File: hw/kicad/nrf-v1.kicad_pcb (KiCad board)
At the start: 2 copper layers, 32 parts, among them U1 TPS62732, U2 nRF51822, U3 SST25WF040B, U4 BMA280, U5 SI7053, U6 BAL-NRF01D3, X1 16MHz, X2 32.768kHz

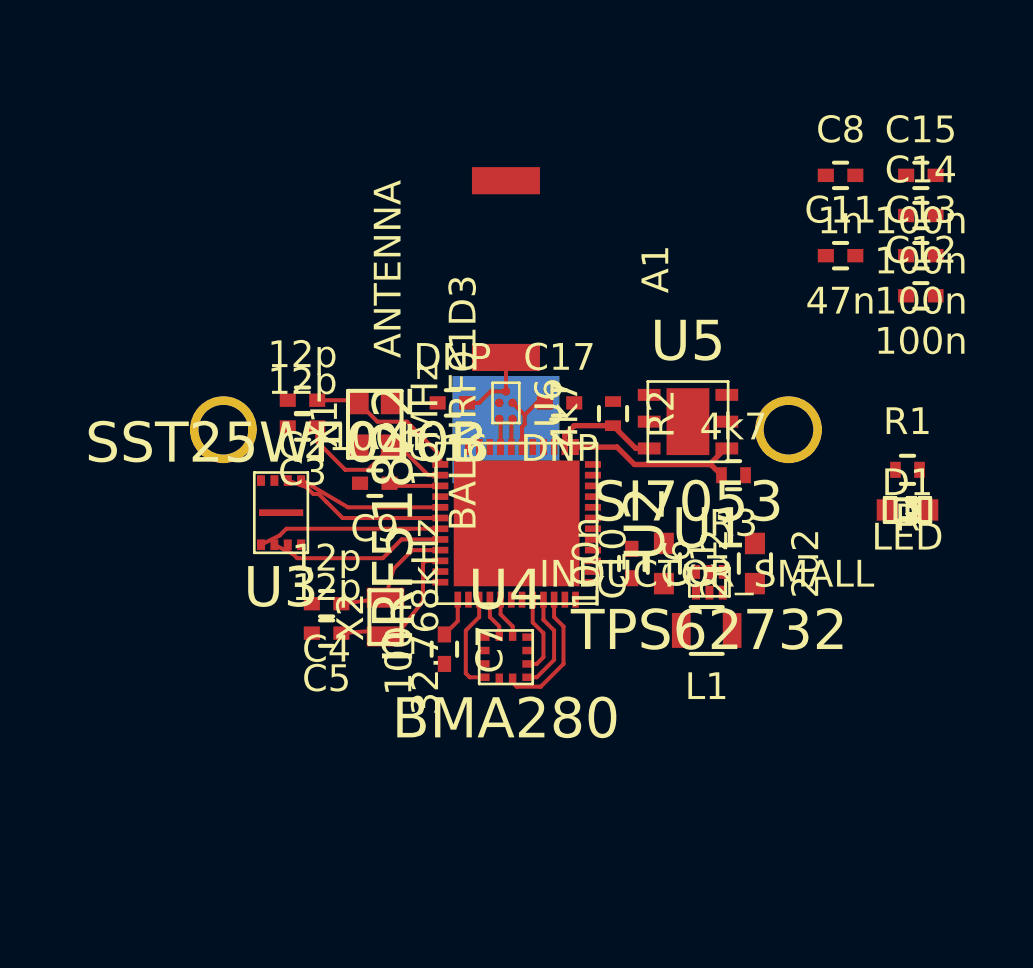
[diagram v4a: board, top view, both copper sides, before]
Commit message: Add PCB shape
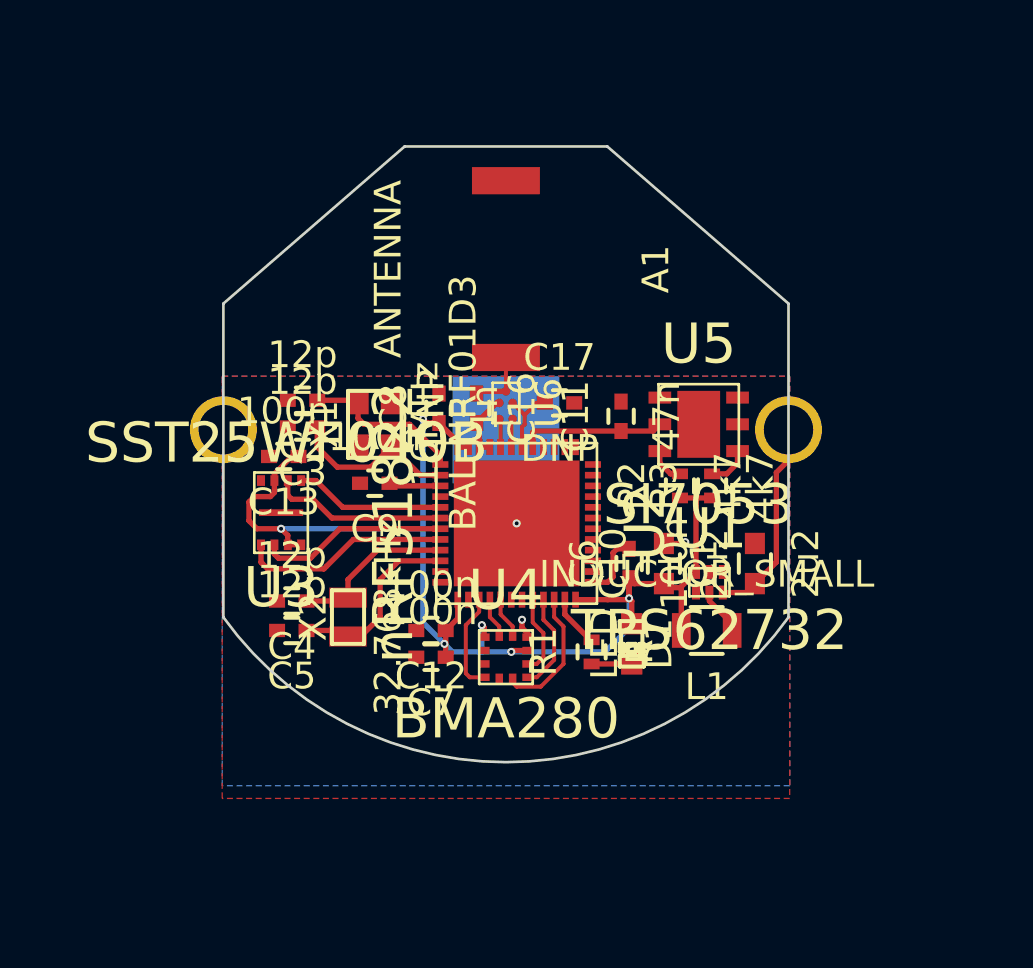
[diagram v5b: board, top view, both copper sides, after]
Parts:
- removed C14, C15: 100n, Capacitors_SMD:C_0402
- moved C13 25.0 mm to (91.7, 101.0), turned to 180 degrees
- moved C12 22.2 mm to (97.2, 107.5), turned to 180 degrees
- moved C8 17.3 mm to (97.5, 99.2), turned to 90 degrees
- moved R1 13.6 mm to (103.2, 108.3), turned to 90 degrees
- moved D1 11.4 mm to (104.7, 108.0), turned to 270 degrees
- moved C11 10.2 mm to (104.3, 99.5), turned to 90 degrees
- moved R2 3.68 mm to (106.5, 102.1), turned to 90 degrees
- moved X2 1.40 mm to (94.1, 107.0)
- moved C4 1.30 mm to (92.0, 106.4)
- moved C5 1.30 mm to (92.0, 107.5)
- moved C16 0.92 mm to (98.9, 99.2), turned to 270 degrees
- moved R3 0.89 mm to (107.7, 102.1), turned to 90 degrees
- moved C7 0.58 mm to (97.2, 108.5), turned to 180 degrees
- moved U5 0.41 mm to (107.2, 99.8)
- moved C6 0.10 mm to (104.6, 105.0), turned to 90 degrees
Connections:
- D1 pad 1: +BATT -> VDD
- U2 pad 11: Net-(U2-Pad11) -> ~led
- U2 pad 43: spi0_mosi -> spi0_sck
- U2 pad 44: spi0_sck -> spi0_mosi
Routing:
- net VDD: track 1.51 -> 54.0 mm, vias 0 -> 6
- net +BATT: track 0.00 -> 7.61 mm
- net GND: track 0.14 -> 6.59 mm, vias 0 -> 3
- net twi_sda: track 6.78 -> 1.57 mm
- net twi_scl: track 4.10 -> 1.37 mm
- net ~led: track 0.00 -> 1.94 mm
- net Net-(L1-Pad1): track 0.00 -> 1.77 mm
- net Net-(D1-Pad2): track 0.00 -> 1.50 mm
- net Net-(C4-Pad1): track 4.83 -> 6.18 mm
- net Net-(C5-Pad1): track 5.89 -> 7.08 mm
- net spi0_mosi: track 6.89 -> 7.91 mm
- added copper zone on B.Cu, net GND
- added copper zone on F.Cu, net GND
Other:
- board outline added: 21.1 x 23 mm

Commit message: Replace temp sensor
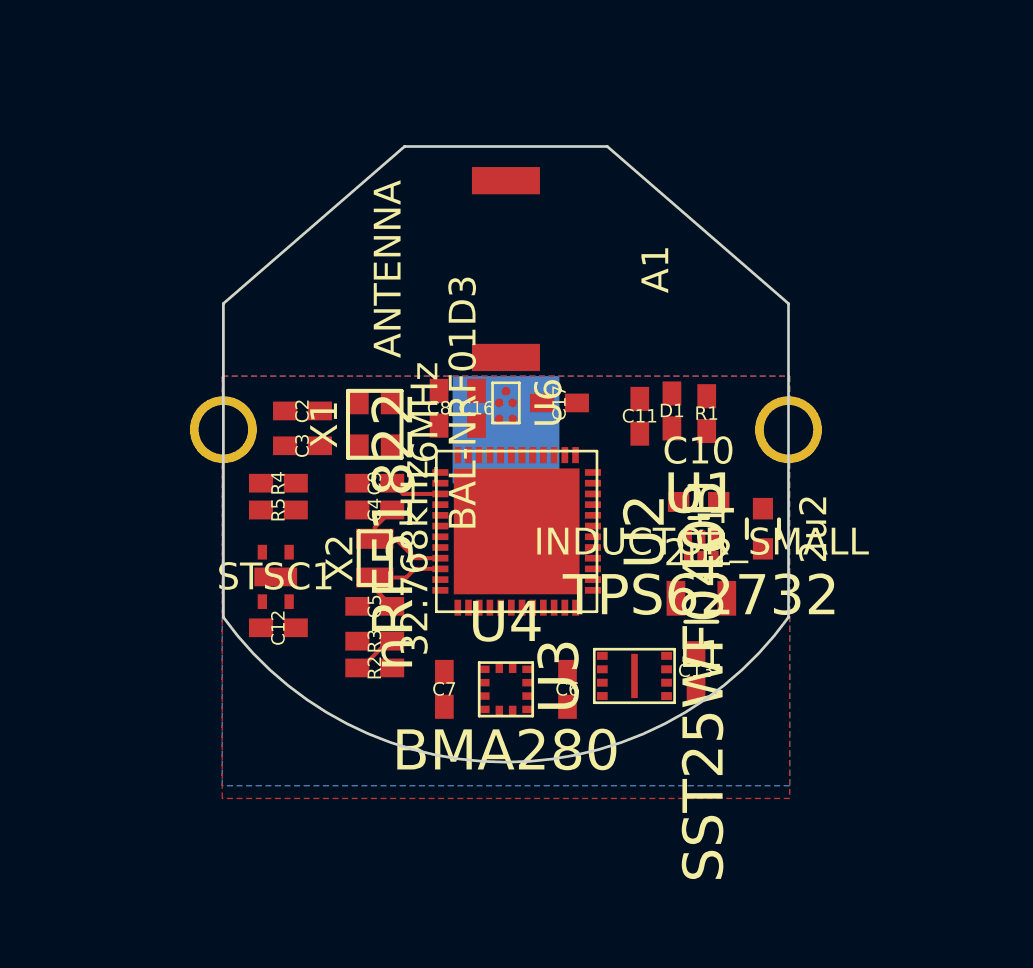
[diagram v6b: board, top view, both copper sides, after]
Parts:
- added R4: 100k, project:IPC-0402, F.Cu at (91.5, 102.0)
- added R5: 120k, project:IPC-0402, F.Cu at (91.5, 103.0)
- C11, C12, C13, C16, C17, C2, C3, C4, C5, C6, C7, C8, C9: footprint Capacitors_SMD:C_0402 -> project:IPC-0402
- D1: footprint LEDs:LED-0603 -> project:IPC-0402
- R1, R2, R3: footprint Resistors_SMD:R_0402 -> project:IPC-0402
- U5: value SI7053 -> STSC1; footprint project:Silabs-DFN-6_(3.00x3.00) -> project:Sensirion-DFN-4_(2.0x2.0)
- moved C13 17.4 mm to (107.1, 109.0), turned to 90 degrees
- moved U5 16.8 mm to (91.4, 105.5), turned to 0 degrees
- moved U3 14.5 mm to (104.8, 109.2), turned to 270 degrees
- moved R3 13.9 mm to (95.1, 107.9), turned to 180 degrees
- moved R2 13.3 mm to (95.1, 108.9), turned to 0 degrees
- moved R1 9.88 mm to (107.5, 99.4)
- moved D1 8.83 mm to (106.2, 99.3), turned to 90 degrees
- moved C12 5.70 mm to (91.5, 107.4)
- moved C6 5.23 mm to (102.3, 109.7), turned to 270 degrees
- moved C4 4.60 mm to (95.1, 103.0)
- moved C5 3.23 mm to (95.1, 106.6)
- moved C10 2.64 mm to (107.2, 102.7), turned to 0 degrees
- moved X2 2.42 mm to (95.1, 104.8)
- moved C1 1.33 mm to (109.6, 103.7)
- moved U1 1.33 mm to (107.3, 104.4)
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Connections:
- U5 pad 1: twi_sda -> VDD
- U5 pad 2: GND -> twi_scl
- U5 pad 3: Net-(U5-Pad3) -> twi_sda
- U5 pad 4: Net-(U5-Pad4) -> GND
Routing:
- net VDD: track 54.0 -> 1.68 mm, vias 6 -> 0
- net spi0_mosi: track 7.91 -> 0.00 mm
- net +BATT: track 7.61 -> 0.00 mm
- net spi0_sck: track 7.07 -> 0.00 mm
- net Net-(C3-Pad1): track 6.73 -> 0.00 mm
- net spi0_miso: track 6.60 -> 0.00 mm
- net GND: track 6.59 -> 0.00 mm, vias 3 -> 0
- net Net-(C2-Pad1): track 6.26 -> 0.00 mm
- net spi0_cs_n: track 5.66 -> 0.00 mm
- net spi1_sck: track 4.99 -> 0.00 mm
- net spi1_cs_n: track 3.70 -> 0.00 mm
- net spi1_miso: track 3.67 -> 0.00 mm
- net Net-(C5-Pad1): track 7.08 -> 3.93 mm
- net spi1_mosi: track 3.00 -> 0.00 mm
- net Net-(C17-Pad1): track 2.81 -> 0.00 mm
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
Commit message: PCB ready for 1st review
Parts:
- added TP1: Testpoint, project:TP_0.6, F.Cu at (108.1, 106.2)
- added TP2: Testpoint, project:TP_0.6, F.Cu at (109.4, 106.2)
- added TP3: Testpoint, project:TP_0.6, F.Cu at (108.1, 107.5)
- added TP4: Testpoint, project:TP_0.6, F.Cu at (109.4, 107.5)
- added TP5: Testpoint, project:TP_0.6, B.Cu at (102.3, 111.0)
- C1, C10: footprint Capacitors_SMD:C_0603 -> project:IPC-0603
- L1: footprint Resistors_SMD:R_0805 -> project:IPC-0805
- moved R5 16.9 mm to (107.9, 98.8), turned to 0 degrees
- moved R4 16.5 mm to (107.9, 100.0), turned to 180 degrees
- moved C12 6.89 mm to (98.0, 109.7), turned to 270 degrees
- moved C1 3.32 mm to (107.3, 101.3), turned to 180 degrees
- moved L1 3.14 mm to (109.2, 103.8), turned to 270 degrees
- moved C11 3.01 mm to (102.0, 99.8), turned to 0 degrees
- moved C5 2.97 mm to (92.6, 105.0)
- moved C4 2.62 mm to (92.6, 103.8)
- moved C7 2.57 mm to (95.2, 109.1), turned to 180 degrees
- moved R1 2.57 mm to (105.0, 100.0), turned to 180 degrees
- moved C9 2.55 mm to (92.6, 102.5)
- moved U5 1.92 mm to (92.3, 107.2), turned to 90 degrees
- moved C10 1.84 mm to (105.6, 103.6), turned to 90 degrees
- moved D1 1.30 mm to (105.0, 98.8), turned to 0 degrees
- moved C16 1.22 mm to (97.9, 98.5), turned to 180 degrees
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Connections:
- U1 pad 5: Net-(U1-Pad5) -> +BATT
- U2 pad 11: ~led -> bootloader
- U2 pad 14: Net-(U2-Pad14) -> spi0_cs_n
- U2 pad 15: Net-(U2-Pad15) -> spi0_miso
- U2 pad 16: Net-(U2-Pad16) -> spi0_sck
- U2 pad 17: Net-(U2-Pad17) -> spi0_mosi
- U2 pad 25: twi_sda -> ~led
- U2 pad 26: twi_scl -> Net-(U2-Pad26)
- U2 pad 41: spi0_cs_n -> Net-(U2-Pad41)
- U2 pad 42: spi0_miso -> Net-(U2-Pad42)
- U2 pad 43: spi0_sck -> Net-(U2-Pad43)
- U2 pad 44: spi0_mosi -> Net-(U2-Pad44)
- U2 pad 47: Net-(U2-Pad47) -> twi_sda
- U2 pad 48: Net-(U2-Pad48) -> twi_scl
- U2 pad 7: Net-(U2-Pad7) -> vbat_adc
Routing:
- net VDD: track 1.68 -> 64.0 mm, vias 0 -> 6
- net GND: track 0.00 -> 19.8 mm, vias 0 -> 3
- net vbat_adc: track 0.00 -> 15.5 mm, vias 0 -> 2
- net swclk: track 0.00 -> 10.4 mm, vias 0 -> 2
- net +BATT: track 0.00 -> 9.26 mm, vias 0 -> 2
- net swdio: track 0.00 -> 8.64 mm, vias 0 -> 2
- net twi_sda: track 0.00 -> 7.55 mm
- net spi1_cs_n: track 0.00 -> 7.20 mm
- net twi_scl: track 0.00 -> 6.28 mm
- net spi1_sck: track 0.00 -> 6.10 mm
- net spi0_miso: track 0.00 -> 5.64 mm
- net Net-(C2-Pad1): track 0.00 -> 5.21 mm
- net spi0_cs_n: track 0.00 -> 5.12 mm
- net Net-(C3-Pad1): track 0.00 -> 5.06 mm
- net spi0_mosi: track 0.00 -> 4.81 mm
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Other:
- net class Default: via_dia 0.3 -> 0.5
- rule via_min_size: 0.3 -> 0.5

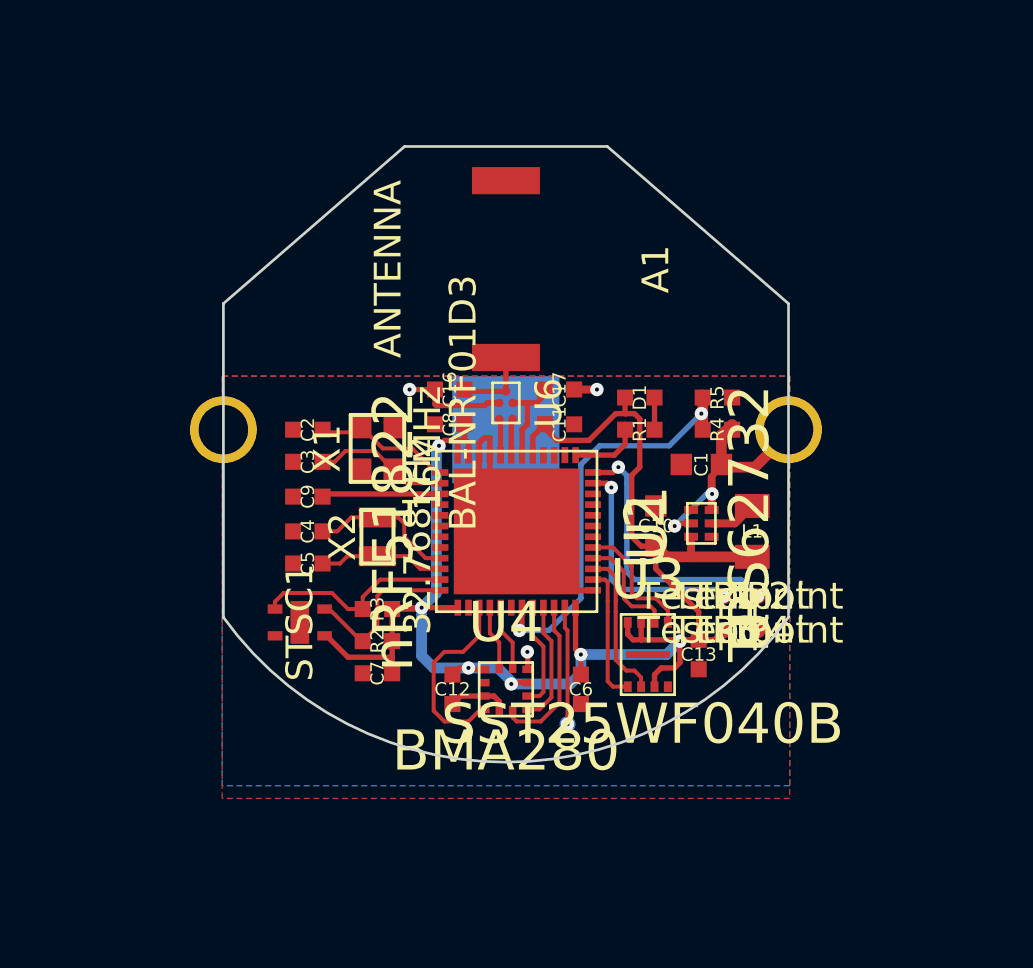
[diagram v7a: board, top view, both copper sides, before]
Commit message: Update layout
- footprint updates
- added gnd vias
- polygon fills (max'd out)
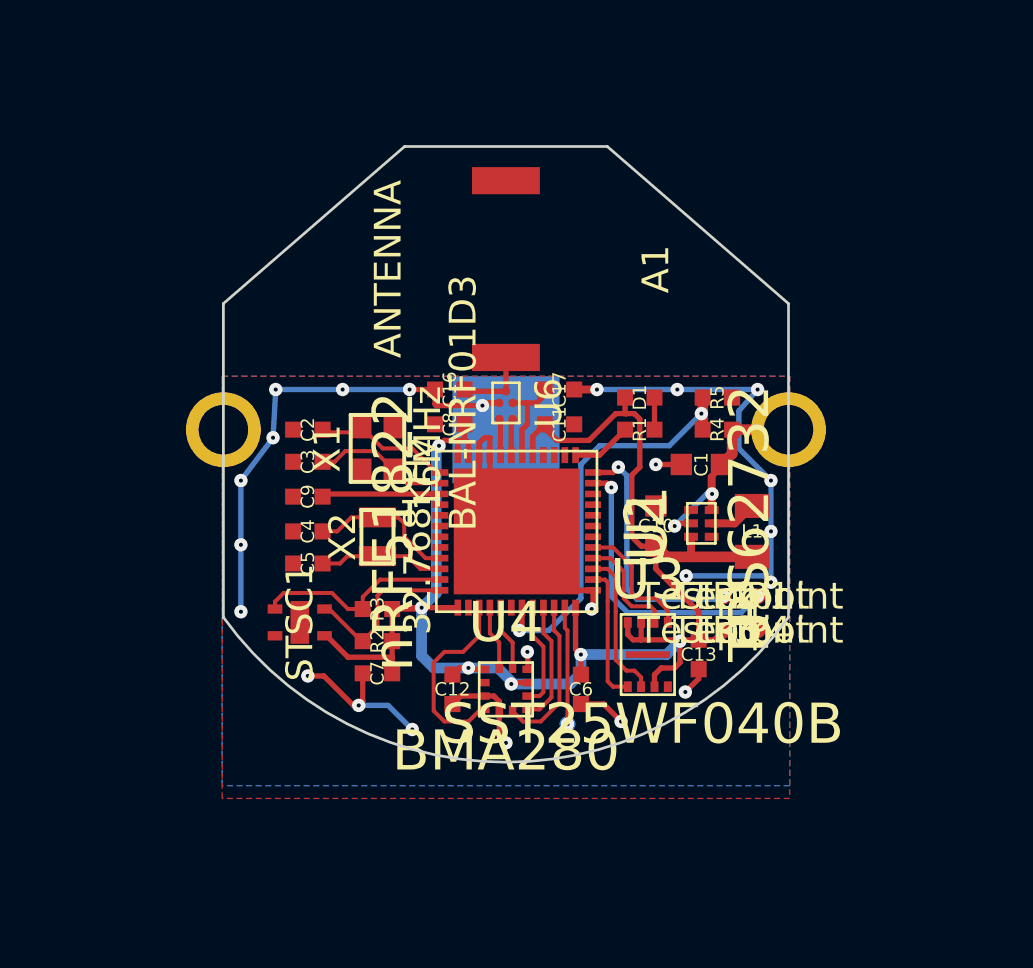
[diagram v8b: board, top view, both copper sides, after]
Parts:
- moved TP1 1.27 mm to (109.4, 106.2)
- moved TP2 1.27 mm to (108.1, 106.2)
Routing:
- net GND: track 19.8 -> 64.6 mm, vias 3 -> 24
- net swdio: track 8.64 -> 10.8 mm
- net +BATT: track 9.26 -> 7.89 mm
- net swclk: track 10.4 -> 9.55 mm
- net ~led: track 2.77 -> 2.24 mm
